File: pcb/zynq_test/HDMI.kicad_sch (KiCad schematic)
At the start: 2 parts, among them J801 HDMI_B, J802 HDMI_B

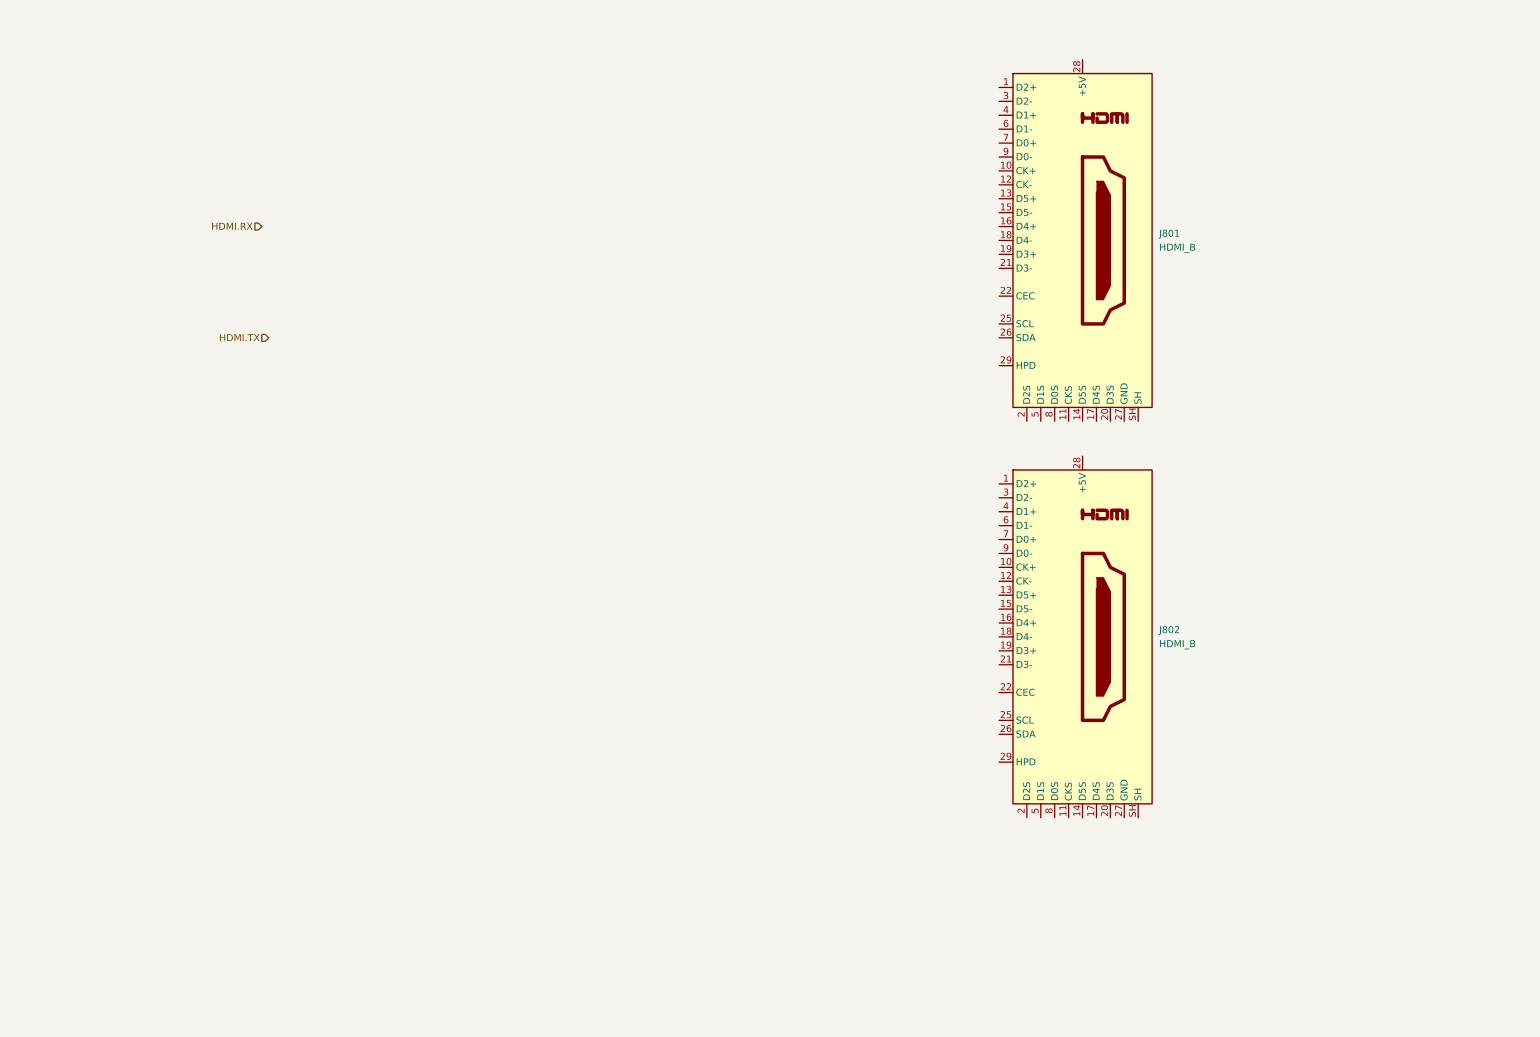
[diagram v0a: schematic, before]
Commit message: Finished HDMI
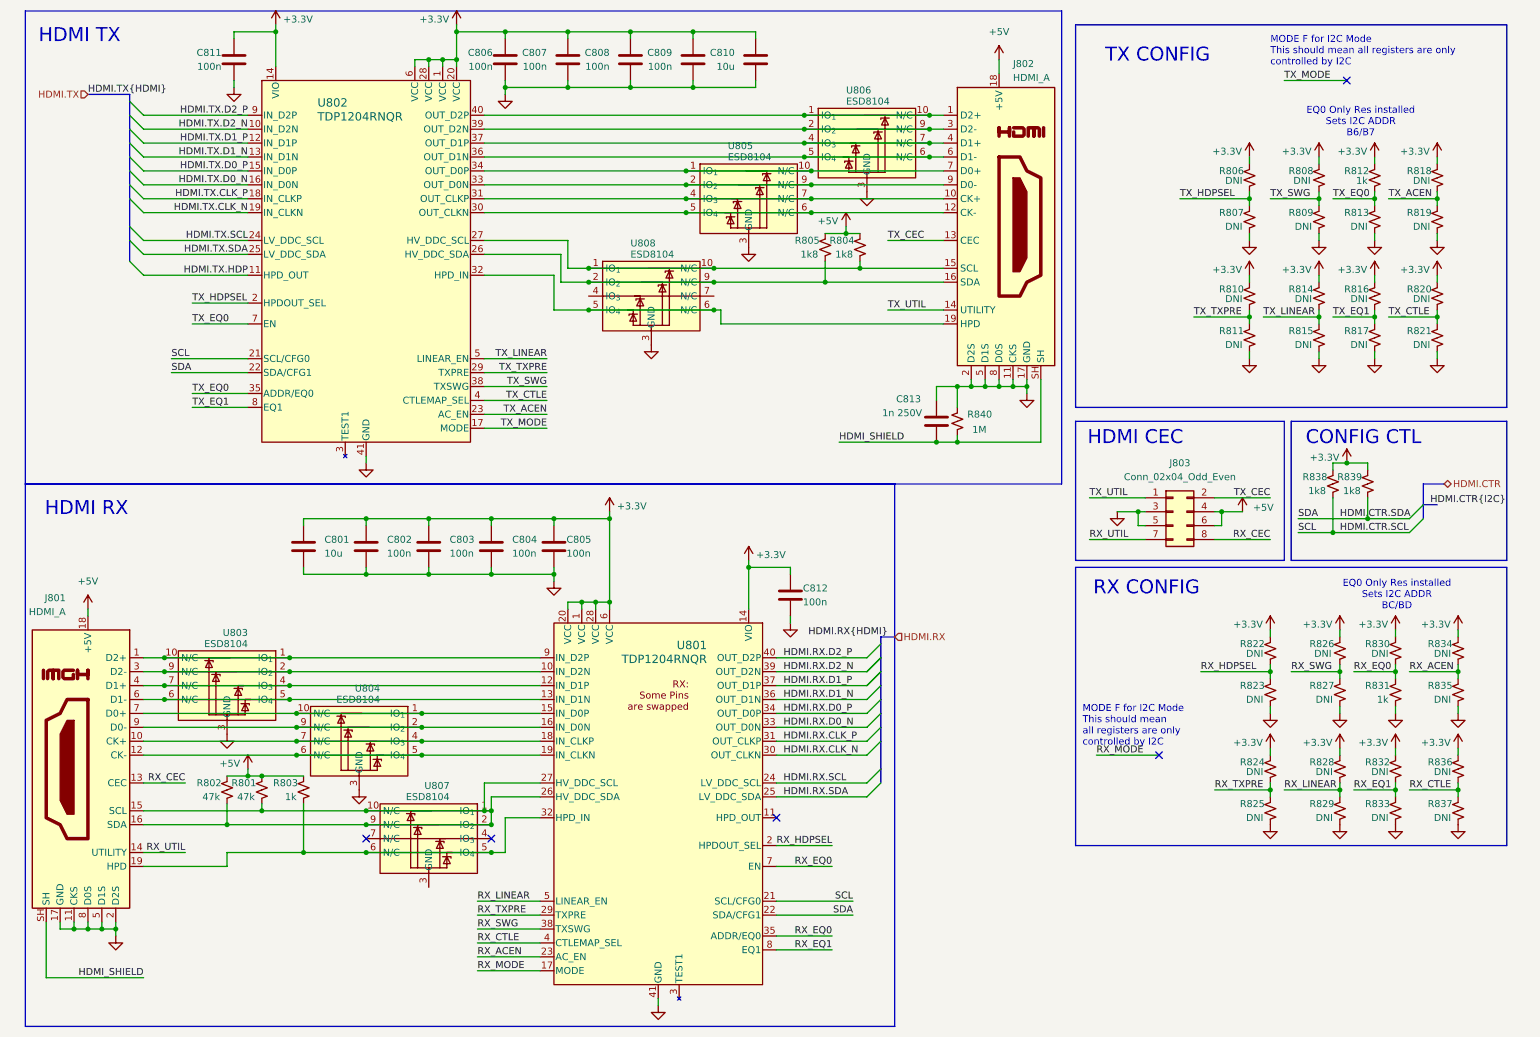
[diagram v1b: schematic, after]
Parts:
- removed J801, J802: HDMI_B, symbol Connector:HDMI_B
- added C801, C810: 10u, symbol Device:C
- added C802, C803, C804, C805, C806, C807, C808, C809, C811, C812: 100n, symbol Device:C
- added C813: 1n 250V, symbol Device:C
- added J801, J802: HDMI_A, Connector_Video:HDMI_A_Amphenol_10029449-x01xLF_Horizontal, symbol Connector:HDMI_A
- added J803: Conn_02x04_Odd_Even, symbol Connector_Generic:Conn_02x04_Odd_Even
- added R801, R802: 47k, symbol Device:R_Small_US
- added R803, R812, R831: 1k, symbol Device:R_Small_US
- added R804, R805, R838, R839: 1k8, symbol Device:R_Small_US
- added R806, R807, R808, R809, R810, R811, R813, R814, R815, R816, R817, R818, R819, R820, R821, R822, R823, R824, R825, R826, R827, R828, R829, R830, R832, R833, R834, R835, R836, R837: DNI, symbol Device:R_Small_US
- added R840: 1M, symbol Device:R_Small_US
- added U801, U802: TDP1204RNQR, Package_DFN_QFN:Texas_RNQ0040A_WQFN-40-1EP_6x4mm_P0.4mm_EP4.7x2.7mm, symbol hdmi:TDP1204RNQR
- added U803, U804, U805, U806, U807, U808: ESD8104, symbol other:ESD8104
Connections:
- new net: J801.3 (D2-), U801.10 (IN_D2N), U803.2 (IO_{2}), U803.9 (N/C)
- new net: J801.4 (D1+), U801.12 (IN_D1P), U803.4 (IO_{3}), U803.7 (N/C)
- new net: J801.6 (D1-), U801.13 (IN_D1N), U803.5 (IO_{4}), U803.6 (N/C)
- new net: J801.7 (D0+), U801.15 (IN_D0P), U804.1 (IO_{1}), U804.10 (N/C)
- new net: J801.9 (D0-), U801.16 (IN_D0N), U804.2 (IO_{2}), U804.9 (N/C)
- new net: J801.10 (CK+), U801.18 (IN_CLKP), U804.4 (IO_{3}), U804.7 (N/C)
- new net: J801.12 (CK-), U801.19 (IN_CLKN), U804.5 (IO_{4}), U804.6 (N/C)
- new net: J801.15 (SCL), J801.16 (SDA), R801.2, R802.2, U801.26 (HV_DDC_SDA), U801.27 (HV_DDC_SCL), U807.1 (IO_{1}), U807.10 (N/C), U807.2 (IO_{2}), U807.9 (N/C)
- new net: J801.19 (HPD), R803.2, U801.32 (HPD_IN), U807.5 (IO_{4}), U807.6 (N/C)
- new net: J801.1 (D2+), U801.9 (IN_D2P), U803.1 (IO_{1}), U803.10 (N/C)
- new net: J802.15 (SCL), R804.2, U802.27 (HV_DDC_SCL), U808.1 (IO_{1}), U808.10 (N/C)
- new net: J802.7 (D0+), U802.34 (OUT_D0P), U805.1 (IO_{1}), U805.10 (N/C)
- new net: J802.9 (D0-), U802.33 (OUT_D0N), U805.2 (IO_{2}), U805.9 (N/C)
- new net: J802.10 (CK+), U802.31 (OUT_CLKP), U805.4 (IO_{3}), U805.7 (N/C)
- new net: J802.12 (CK-), U802.30 (OUT_CLKN), U805.5 (IO_{4}), U805.6 (N/C)
- new net: J802.16 (SDA), R805.2, U802.26 (HV_DDC_SDA), U808.2 (IO_{2}), U808.9 (N/C)
- new net: J802.19 (HPD), U802.32 (HPD_IN), U808.5 (IO_{4}), U808.6 (N/C)
- new net: J802.6 (D1-), U802.36 (OUT_D1N), U806.5 (IO_{4}), U806.6 (N/C)
- new net: J802.4 (D1+), U802.37 (OUT_D1P), U806.4 (IO_{3}), U806.7 (N/C)
- new net: J802.3 (D2-), U802.39 (OUT_D2N), U806.2 (IO_{2}), U806.9 (N/C)
- new net: J802.1 (D2+), U802.40 (OUT_D2P), U806.1 (IO_{1}), U806.10 (N/C)
- new net +3.3V: C801.1, C802.1, C803.1, C804.1, C805.1, C806.1, C807.1, C808.1, C809.1, C810.1, C811.1, C812.1, R806.1, R808.1, R810.1, R812.1, R814.1, R816.1, R818.1, R820.1, R822.1, R824.1, R826.1, R828.1, R830.1, R832.1, R834.1, R836.1, R838.1, R839.1, U801.1 (VCC), U801.14 (VIO), U801.20 (VCC), U801.28 (VCC), U801.6 (VCC), U802.1 (VCC), U802.14 (VIO), U802.20 (VCC), U802.28 (VCC), U802.6 (VCC)
- new net +5V: J801.18 (+5V), J802.18 (+5V), J803.4 (Pin_4), J803.6 (Pin_6), R801.1, R802.1, R803.1, R804.1, R805.1
- new net GND: C801.2, C802.2, C803.2, C804.2, C805.2, C806.2, C807.2, C808.2, C809.2, C810.2, C811.2, C812.2, C813.1, J801.11 (CKS), J801.17 (GND), J801.2 (D2S), J801.5 (D1S), J801.8 (D0S), J802.11 (CKS), J802.17 (GND), J802.2 (D2S), J802.5 (D1S), J802.8 (D0S), J803.3 (Pin_3), J803.5 (Pin_5), R807.2, R809.2, R811.2, R813.2, R815.2, R817.2, R819.2, R821.2, R823.2, R825.2, R827.2, R829.2, R831.2, R833.2, R835.2, R837.2, R840.1, U801.41 (GND), U802.41 (GND), U803.3 (GND), U804.3 (GND), U805.3 (GND), U806.3 (GND), U808.3 (GND)
- new net HDMI.CTR.SCL: R838.2, U801.21 (SCL/CFG0), U802.21 (SCL/CFG0)
- new net HDMI.CTR.SDA: R839.2, U801.22 (SDA/CFG1), U802.22 (SDA/CFG1)
- new net HDMI.RX.CLK_N: U801.30 (OUT_CLKN)
- new net HDMI.RX.CLK_P: U801.31 (OUT_CLKP)
- new net HDMI.RX.D0_N: U801.33 (OUT_D0N)
- new net HDMI.RX.D0_P: U801.34 (OUT_D0P)
- new net HDMI.RX.D1_N: U801.36 (OUT_D1N)
- new net HDMI.RX.D1_P: U801.37 (OUT_D1P)
- new net HDMI.RX.D2_N: U801.39 (OUT_D2N)
- new net HDMI.RX.D2_P: U801.40 (OUT_D2P)
- new net HDMI.RX.SCL: U801.24 (LV_DDC_SCL)
- new net HDMI.RX.SDA: U801.25 (LV_DDC_SDA)
- new net HDMI.TX.CLK_N: U802.19 (IN_CLKN)
- new net HDMI.TX.CLK_P: U802.18 (IN_CLKP)
- new net HDMI.TX.D0_N: U802.16 (IN_D0N)
- new net HDMI.TX.D0_P: U802.15 (IN_D0P)
- new net HDMI.TX.D1_N: U802.13 (IN_D1N)
- new net HDMI.TX.D1_P: U802.12 (IN_D1P)
- new net HDMI.TX.D2_N: U802.10 (IN_D2N)
- new net HDMI.TX.D2_P: U802.9 (IN_D2P)
- new net HDMI.TX.HDP: U802.11 (HPD_OUT)
- new net HDMI.TX.SCL: U802.24 (LV_DDC_SCL)
- new net HDMI.TX.SDA: U802.25 (LV_DDC_SDA)
- new net HDMI_SHIELD: C813.2, J801.SH, J802.SH, R840.2
- new net RX_ACEN: R834.2, R835.1, U801.23 (AC_EN)
- new net RX_CEC: J801.13 (CEC), J803.8 (Pin_8)
- new net RX_CTLE: R836.2, R837.1, U801.4 (CTLEMAP_SEL)
- new net RX_EQ0: R830.2, R831.1, U801.35 (ADDR/EQ0), U801.7 (EN)
- new net RX_EQ1: R832.2, R833.1, U801.8 (EQ1)
- new net RX_HDPSEL: R822.2, R823.1, U801.2 (HPDOUT_SEL)
- new net RX_LINEAR: R828.2, R829.1, U801.5 (LINEAR_EN)
- new net RX_MODE: U801.17 (MODE)
- new net RX_SWG: R826.2, R827.1, U801.38 (TXSWG)
- new net RX_TXPRE: R824.2, R825.1, U801.29 (TXPRE)
- new net RX_UTIL: J801.14 (UTILITY), J803.7 (Pin_7)
- new net TX_ACEN: R818.2, R819.1, U802.23 (AC_EN)
- new net TX_CEC: J802.13 (CEC), J803.2 (Pin_2)
- new net TX_CTLE: R820.2, R821.1, U802.4 (CTLEMAP_SEL)
- new net TX_EQ0: R812.2, R813.1, U802.35 (ADDR/EQ0), U802.7 (EN)
- new net TX_EQ1: R816.2, R817.1, U802.8 (EQ1)
- new net TX_HDPSEL: R806.2, R807.1, U802.2 (HPDOUT_SEL)
- new net TX_LINEAR: R814.2, R815.1, U802.5 (LINEAR_EN)
- new net TX_MODE: U802.17 (MODE)
- new net TX_SWG: R808.2, R809.1, U802.38 (TXSWG)
- new net TX_TXPRE: R810.2, R811.1, U802.29 (TXPRE)
- new net TX_UTIL: J802.14 (UTILITY), J803.1 (Pin_1)
- no-connect marks 0 -> 5
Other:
- note added: "CONFIG CTL"
- note added: "EQ0 Only Res installed Sets I2C ADDR B6/B7"
- note added: "EQ0 Only Res installed Sets I2C ADDR BC/BD"
- note added: "HDMI CEC"
- note added: "HDMI RX"
- note added: "HDMI TX"
- note added: "MODE F for I2C Mode This should mean all registers are only controlled by I2C"
- note added: "RX CONFIG"
- note added: "TX CONFIG"

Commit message: Connected DDR3, cleaned up some thing
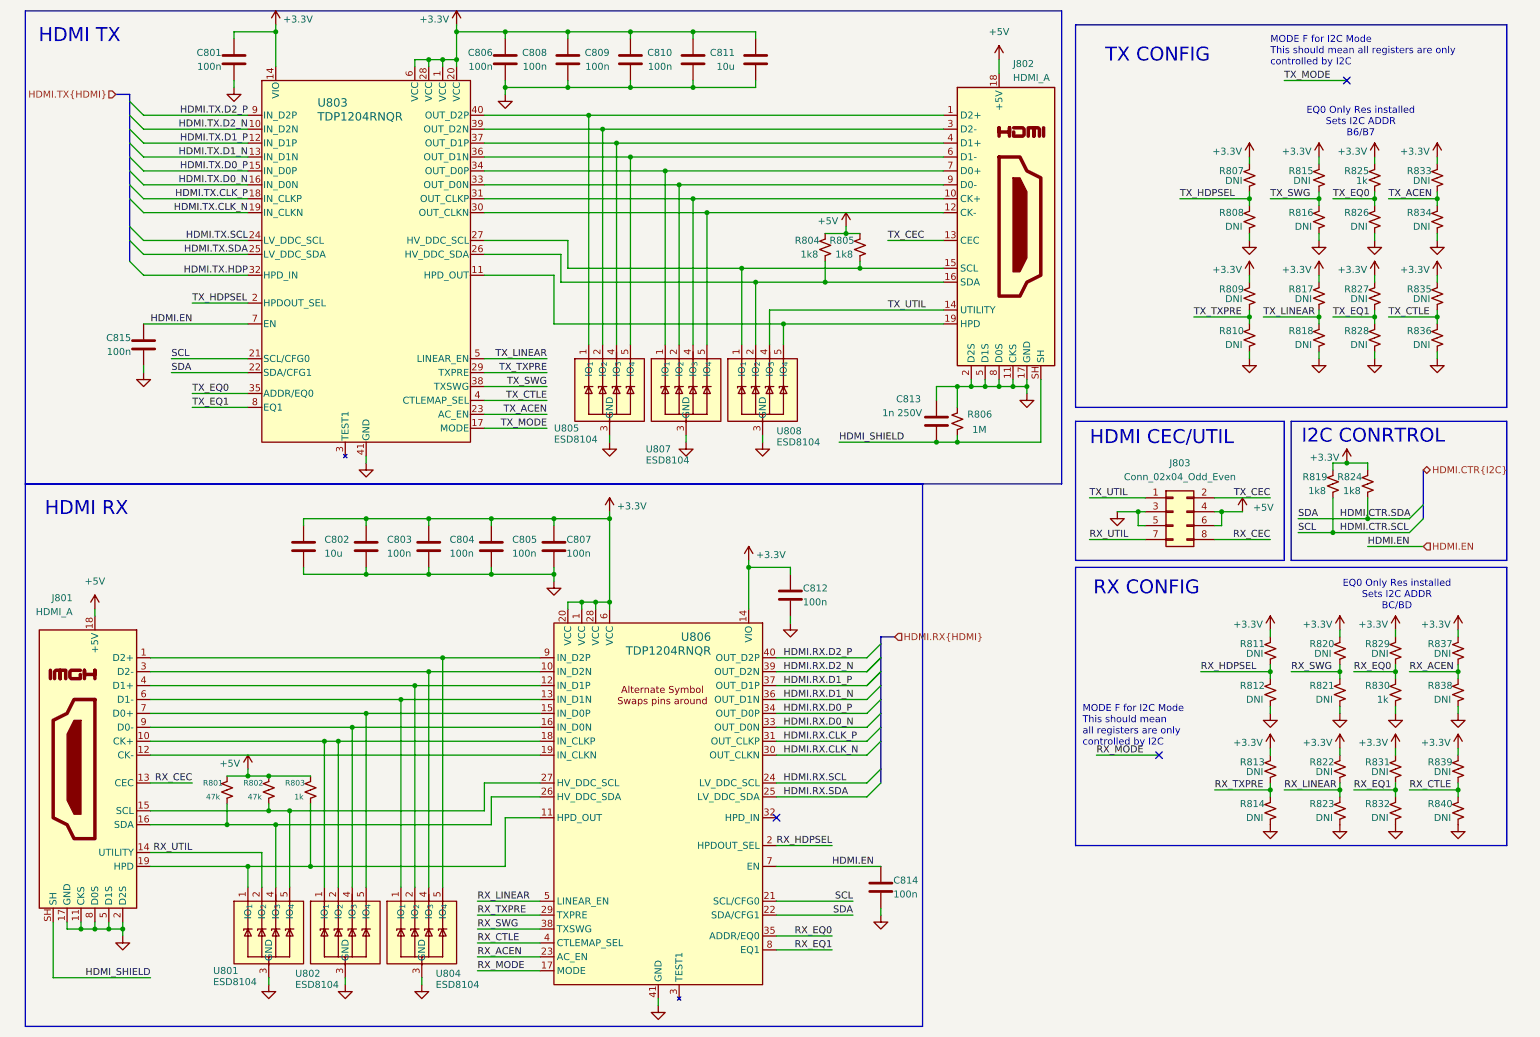
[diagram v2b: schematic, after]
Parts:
- removed U803, U807: ESD8104, symbol other:ESD8104
- added C814, C815: 100n, symbol Device:C
- added U801, U802: ESD8104, symbol other:ESD8104
- U803: renamed from U802; footprint Package_DFN_QFN:Texas_RNQ0040A_WQFN-40-1EP_6x4mm_P0.4mm_EP4.7x2.7mm -> WQFN40_RNQ_TEX
- U806: renamed from U801; footprint Package_DFN_QFN:Texas_RNQ0040A_WQFN-40-1EP_6x4mm_P0.4mm_EP4.7x2.7mm -> WQFN40_RNQ_TEX; symbol hdmi:TDP1204RNQR -> hdmi:TDP1204RNQR_(ALT)
- renumbered C811 to C801, C801 to C802, C802 to C803, C803 to C804, C804 to C805, C805 to C807, C807 to C808, C808 to C809, C809 to C810, C810 to C811, R802 to R801, R801 to R802, R805 to R804, R804 to R805, R840 to R806, R806 to R807, R807 to R808, R810 to R809, R811 to R810, R822 to R811, R823 to R812, R824 to R813, R825 to R814, R808 to R815, R809 to R816, R814 to R817, R815 to R818, R838 to R819, R826 to R820, R827 to R821, R828 to R822, R829 to R823, R839 to R824, R812 to R825, R813 to R826, R816 to R827, R817 to R828, R830 to R829, R831 to R830, R832 to R831, R833 to R832, R818 to R833, R819 to R834, R820 to R835, R821 to R836, R834 to R837, R835 to R838, R836 to R839, R837 to R840, U808 to U805, U805 to U807, U806 to U808
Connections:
- net GND: now also U804.8 (GND), U805.8 (GND), U807.8 (GND), U808.8 (GND), C814.2, C815.2, U801.3 (GND), U801.8 (GND), U802.3 (GND), U802.8 (GND)
- net HDMI.TX.HDP: now also U803.32 (HPD_IN); no longer U803.11 (HPD_OUT)
- net RX_EQ0: no longer U806.7 (EN)
- net RX_UTIL: now also U801.2 (IO_{2}), U801.9 (N/C)
- net TX_EQ0: no longer U803.7 (EN)
- net TX_UTIL: now also U808.4 (IO_{3}), U808.7 (N/C)
- net at J801.3 (D2-), U806.10 (IN_D2N): now also U804.4 (IO_{3}), U804.7 (N/C)
- net at U806.11 (HPD_OUT): now also J801.19 (HPD), R803.2, U801.1 (IO_{1}), U801.10 (N/C)
- net at J801.4 (D1+), U806.12 (IN_D1P): now also U804.2 (IO_{2}), U804.9 (N/C)
- net at J801.6 (D1-), U806.13 (IN_D1N): now also U804.1 (IO_{1}), U804.10 (N/C)
- net at J801.7 (D0+), U806.15 (IN_D0P): now also U802.5 (IO_{4}), U802.6 (N/C); no longer U804.1 (IO_{1}), U804.10 (N/C)
- net at J801.9 (D0-), U806.16 (IN_D0N): now also U802.4 (IO_{3}), U802.7 (N/C); no longer U804.2 (IO_{2}), U804.9 (N/C)
- net at J801.10 (CK+), U806.18 (IN_CLKP): now also U802.1 (IO_{1}), U802.10 (N/C), U802.2 (IO_{2}), U802.9 (N/C); no longer U804.4 (IO_{3}), U804.7 (N/C)
- net at J801.12 (CK-), U806.19 (IN_CLKN): no longer U804.5 (IO_{4}), U804.6 (N/C)
- net at J801.16 (SDA), R801.2, U806.26 (HV_DDC_SDA): now also U801.4 (IO_{3}), U801.7 (N/C); no longer J801.15 (SCL), R802.2, U806.27 (HV_DDC_SCL)
- net at J801.1 (D2+), U806.9 (IN_D2P): now also U804.5 (IO_{4}), U804.6 (N/C)
- net at J802.15 (SCL), R805.2, U803.27 (HV_DDC_SCL): now also U808.1 (IO_{1}), U808.10 (N/C); no longer U805.1 (IO_{1}), U805.10 (N/C)
- net at J802.16 (SDA), R804.2, U803.26 (HV_DDC_SDA): now also U808.2 (IO_{2}), U808.9 (N/C); no longer U805.2 (IO_{2}), U805.9 (N/C)
- net at U805.5 (IO_{4}), U805.6 (N/C): now also J802.6 (D1-), U803.36 (OUT_D1N); no longer J802.19 (HPD), U803.32 (HPD_IN)
- net at U808.5 (IO_{4}), U808.6 (N/C): now also J802.19 (HPD), U803.11 (HPD_OUT); no longer J802.6 (D1-), U803.36 (OUT_D1N)
- net at J802.4 (D1+), U803.37 (OUT_D1P): now also U805.4 (IO_{3}), U805.7 (N/C); no longer U808.4 (IO_{3}), U808.7 (N/C)
- net at J802.3 (D2-), U803.39 (OUT_D2N): now also U805.2 (IO_{2}), U805.9 (N/C); no longer U808.2 (IO_{2}), U808.9 (N/C)
- net at J802.1 (D2+), U803.40 (OUT_D2P): now also U805.1 (IO_{1}), U805.10 (N/C); no longer U808.1 (IO_{1}), U808.10 (N/C)
- new net: J801.15 (SCL), R802.2, U801.5 (IO_{4}), U801.6 (N/C), U806.27 (HV_DDC_SCL)
- new net HDMI.EN: C814.1, C815.1, U803.7 (EN), U806.7 (EN)
- now unconnected: U806.32 (HPD_IN)
- no-connect marks 5 -> 3
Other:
- note added: "HDMI CEC/UTIL"
- note added: "I2C CONRTROL"
- note removed: "CONFIG CTL"
- note removed: "HDMI CEC"
- moved on the sheet: J801, R802, R803

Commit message: Finished Power Supply
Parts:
- U803, U806: footprint WQFN40_RNQ_TEX -> Package_DFN_QFN:Texas_RNQ0040A_WQFN-40-1EP_6x4mm_P0.4mm_EP4.7x2.7mm
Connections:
- net at J801.19 (HPD), R803.2, U801.1 (IO_{1})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: now also U806.32 (HPD_IN); no longer U806.11 (HPD_OUT)
- net +3.3V renamed +3V3
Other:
- title: (none) -> HDMI
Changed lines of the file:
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@@
 	(paper "A4")
 	(title_block
-		(date "2025-09-06")
-		(rev "v1.0")
+		(title "HDMI")
+		(date "2025-09-13")
+		(rev "A")
 	)
 	(bus_alias "HDMI"
@@
 	(rectangle
 		(start 12.7 99.06)
-		(end 176.53 198.12)
+		(end 201.93 198.12)
 		(stroke
 			(width 0)
@@
 	(bus
 		(pts
-			(xy 168.91 127) (xy 171.45 127)
+			(xy 168.91 127) (xy 176.53 127)
 		)
 		(stroke
@@
 	(hierarchical_label "HDMI.RX{HDMI}"
 		(shape input)
-		(at 171.45 127 0)
+		(at 176.53 127 0)
 		(effects
 			(font
@@
 			)
 		)
-		(property "Value" "+3.3V"
+		(property "Value" "+3V3"
 			(at 248.666 124.714 0)
 			(effects
@@
 			)
 		)
-		(property "Footprint" "WQFN40_RNQ_TEX"
+		(property "Footprint" "Package_DFN_QFN:Texas_RNQ0040A_WQFN-40-1EP_6x4mm_P0.4mm_EP4.7x2.7mm"
 			(at 128.27 134.62 0)
 			(effects
@@
 			)
 		)
-		(property "Value" "+3.3V"
+		(property "Value" "+3V3"
 			(at 270.256 146.304 0)
 			(effects
@@
 			)
 		)
-		(property "Value" "+3.3V"
+		(property "Value" "+3V3"
 			(at 62.484 14.224 0)
 			(effects
@@
 			)
 		)
-		(property "Value" "+3.3V"
+		(property "Value" "+3V3"
 			(at 148.844 112.014 0)
 			(effects
@@
 			)
 		)
-		(property "Value" "+3.3V"
+		(property "Value" "+3V3"
 			(at 87.376 14.224 0)
 			(effects
@@
 			)
 		)
-		(property "Value" "+3.3V"
+		(property "Value" "+3V3"
 			(at 244.856 38.354 0)
 			(effects
@@
 			)
 		)
-		(property "Value" "+3.3V"
+		(property "Value" "+3V3"
 			(at 270.256 124.714 0)
 			(effects
@@
 			)
 		)
-		(property "Value" "+3.3V"
+		(property "Value" "+3V3"
 			(at 266.446 59.944 0)
 			(effects
@@
 			)
 		)
-		(property "Value" "+3.3V"
+		(property "Value" "+3V3"
 			(at 232.156 38.354 0)
 			(effects
@@
 			)
 		)
-		(property "Value" "+3.3V"
+		(property "Value" "+3V3"
 			(at 255.016 38.354 0)
 			(effects
@@
 			)
 		)
-		(property "Value" "+3.3V"
+		(property "Value" "+3V3"
 			(at 232.156 59.944 0)
 			(effects
@@
 			)
 		)
-		(property "Value" "+3.3V"
+		(property "Value" "+3V3"
 			(at 255.016 59.944 0)
 			(effects
@@
 			)
 		)
-		(property "Value" "+3.3V"
+		(property "Value" "+3V3"
 			(at 258.826 124.714 0)
 			(effects
@@
 			)
 		)
-		(property "Footprint" "WQFN40_RNQ_TEX"
+		(property "Footprint" "Package_DFN_QFN:Texas_RNQ0040A_WQFN-40-1EP_6x4mm_P0.4mm_EP4.7x2.7mm"
 			(at 43.942 20.574 0)
 			(effects
@@
 			)
 		)
-		(property "Value" "+3.3V"
+		(property "Value" "+3V3"
 			(at 235.966 146.304 0)
 			(effects
@@
 			)
 		)
-		(property "Value" "+3.3V"
+		(property "Value" "+3V3"
 			(at 235.966 124.714 0)
 			(effects
@@
 			)
 		)
-		(property "Value" "+3.3V"
+		(property "Value" "+3V3"
 			(at 249.936 94.234 0)
 			(effects
@@
 			)
 		)
-		(property "Value" "+3.3V"
+		(property "Value" "+3V3"
 			(at 258.826 146.304 0)
 			(effects
@@
 			)
 		)
-		(property "Value" "+3.3V"
+		(property "Value" "+3V3"
 			(at 244.856 59.944 0)
 			(effects
@@
 			)
 		)
-		(property "Value" "+3.3V"
+		(property "Value" "+3V3"
 			(at 123.444 103.124 0)
 			(effects
@@
 			)
 		)
-		(property "Value" "+3.3V"
+		(property "Value" "+3V3"
 			(at 266.446 38.354 0)
 			(effects
@@
 			)
 		)
-		(property "Value" "+3.3V"
+		(property "Value" "+3V3"
 			(at 248.666 146.304 0)
 			(effects
